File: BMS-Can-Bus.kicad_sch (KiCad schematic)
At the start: 23 parts, among them J1 Conn_01x05, Q3 Q_PMOS_GSD, Q4 Q_PMOS_GSD, Q5 Q_PMOS_GSD, Q6 Q_PMOS_GSD, U1 BQ76952PFB

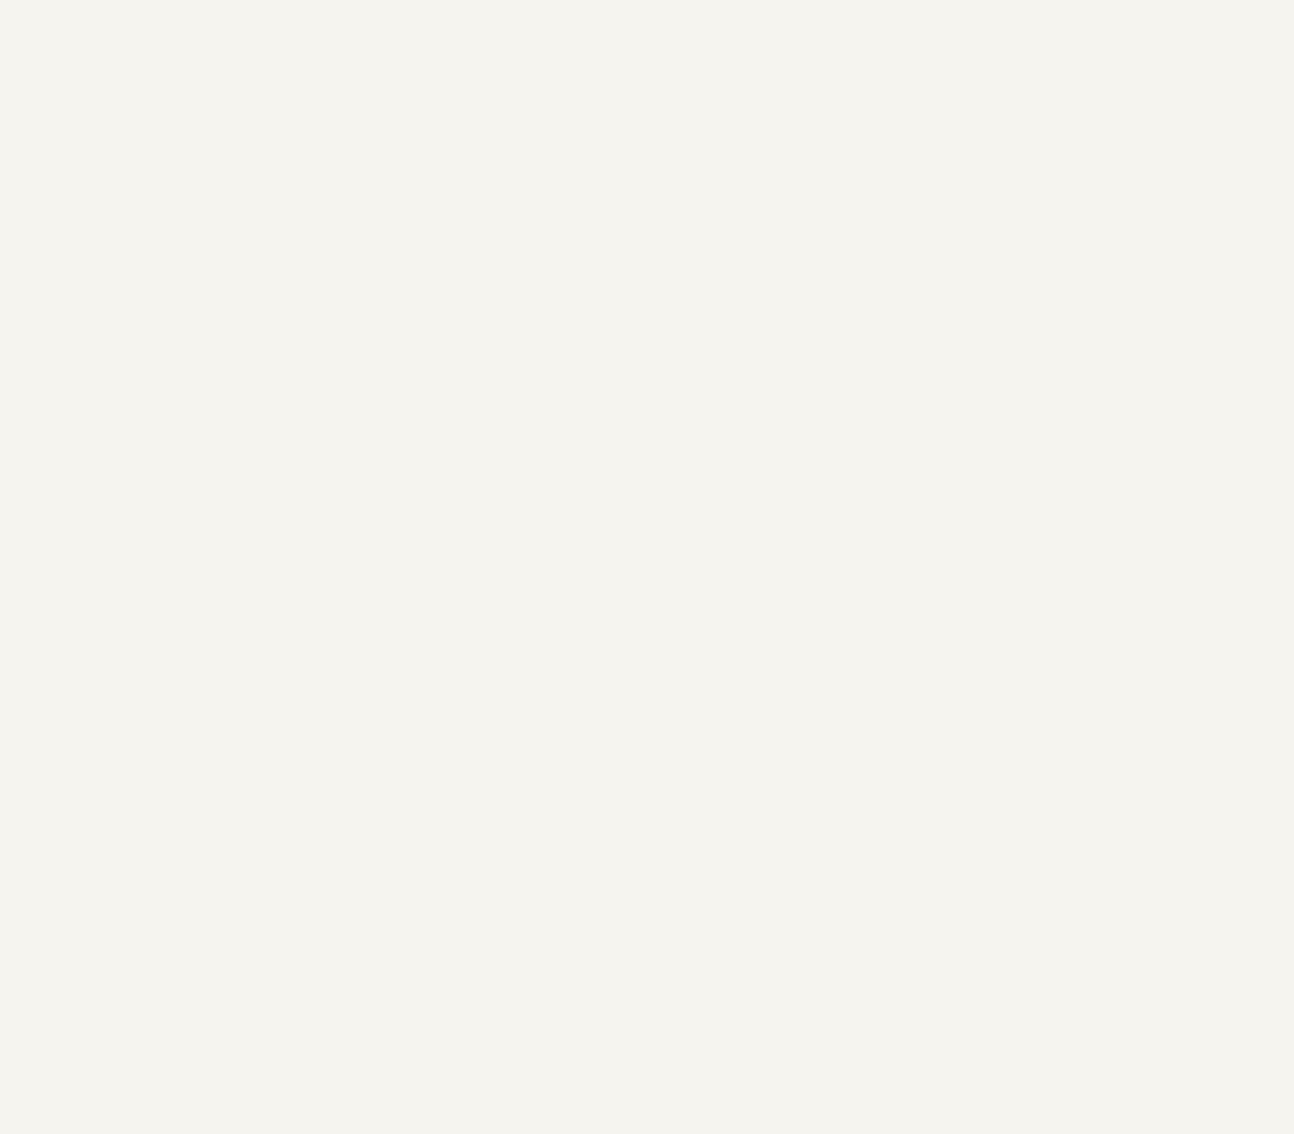
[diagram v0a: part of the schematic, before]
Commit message: Add files via upload
Added STM32 and CAN Bus communication to schematic and PCB.
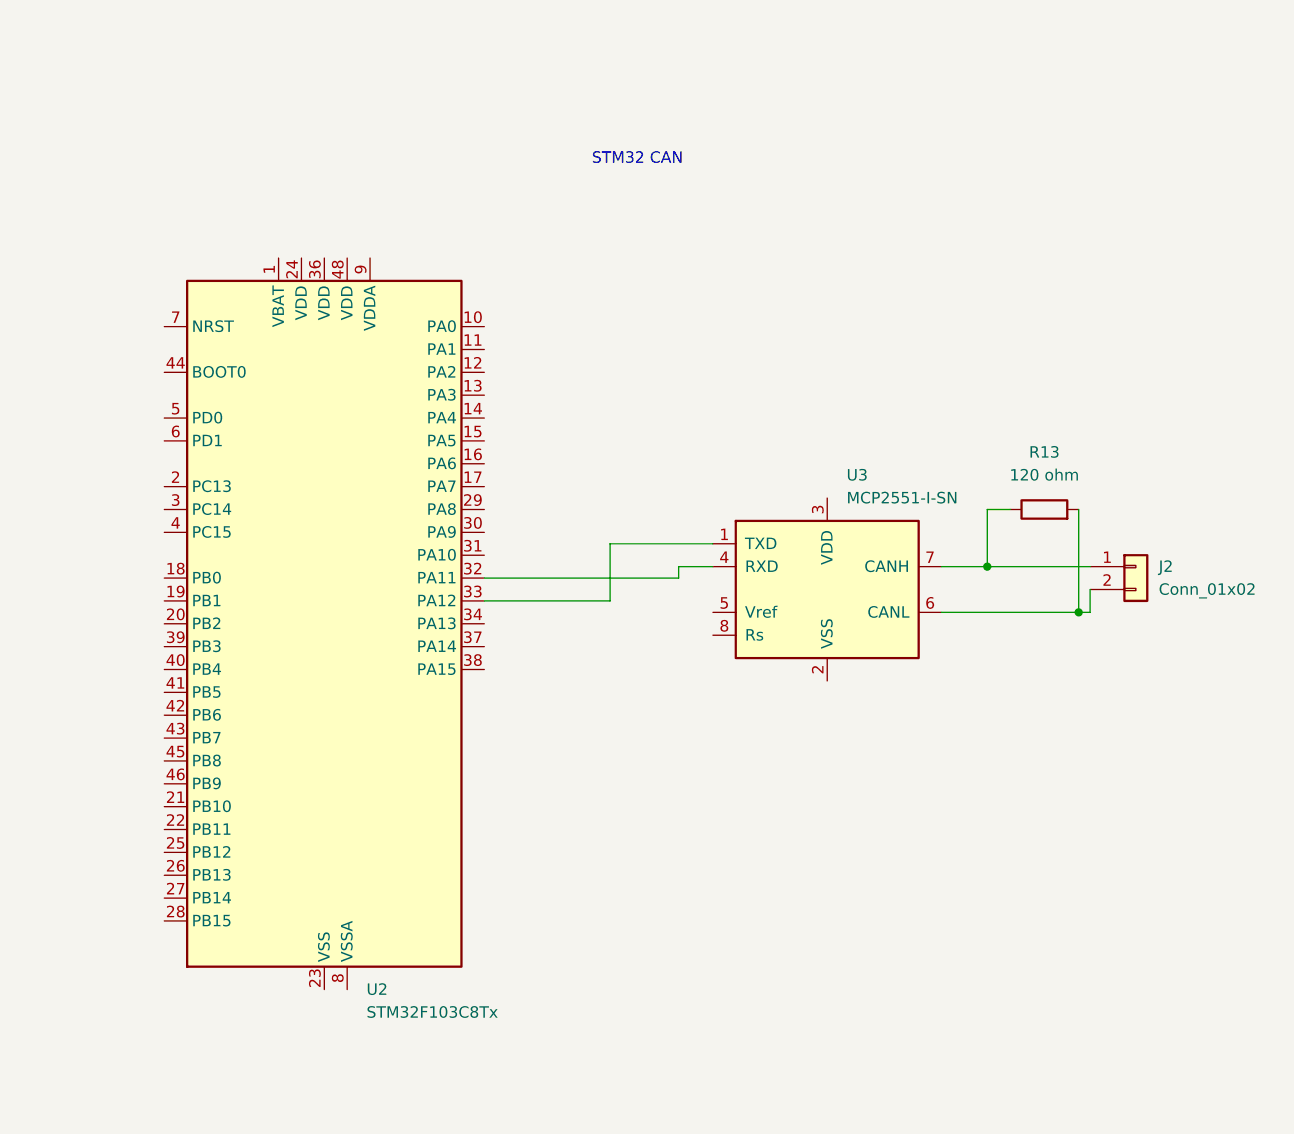
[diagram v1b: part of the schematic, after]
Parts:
- added J2: Conn_01x02, Connector_PinHeader_2.54mm:PinHeader_1x02_P2.54mm_Vertical, symbol Connector_Generic:Conn_01x02
- added R13: 120 ohm, Resistor_SMD:R_0805_2012Metric, symbol Device:R
- added U2: STM32F103C8Tx, Package_QFP:LQFP-48_7x7mm_P0.5mm, symbol MCU_ST_STM32F1:STM32F103C8Tx
- added U3: MCP2551-I-SN, Package_SO:SOIC-8_3.9x4.9mm_P1.27mm, symbol Interface_CAN_LIN:MCP2551-I-SN
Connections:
- new net: U2.33 (PA12), U3.1 (TXD)
- new net: U2.32 (PA11), U3.4 (RXD)
- new net: J2.2 (Pin_2), R13.2, U3.6 (CANL)
- new net: J2.1 (Pin_1), R13.1, U3.7 (CANH)
- new net: U2.23 (VSS), U2.35 (VSS), U2.47 (VSS)
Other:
- note added: "STM32 CAN"

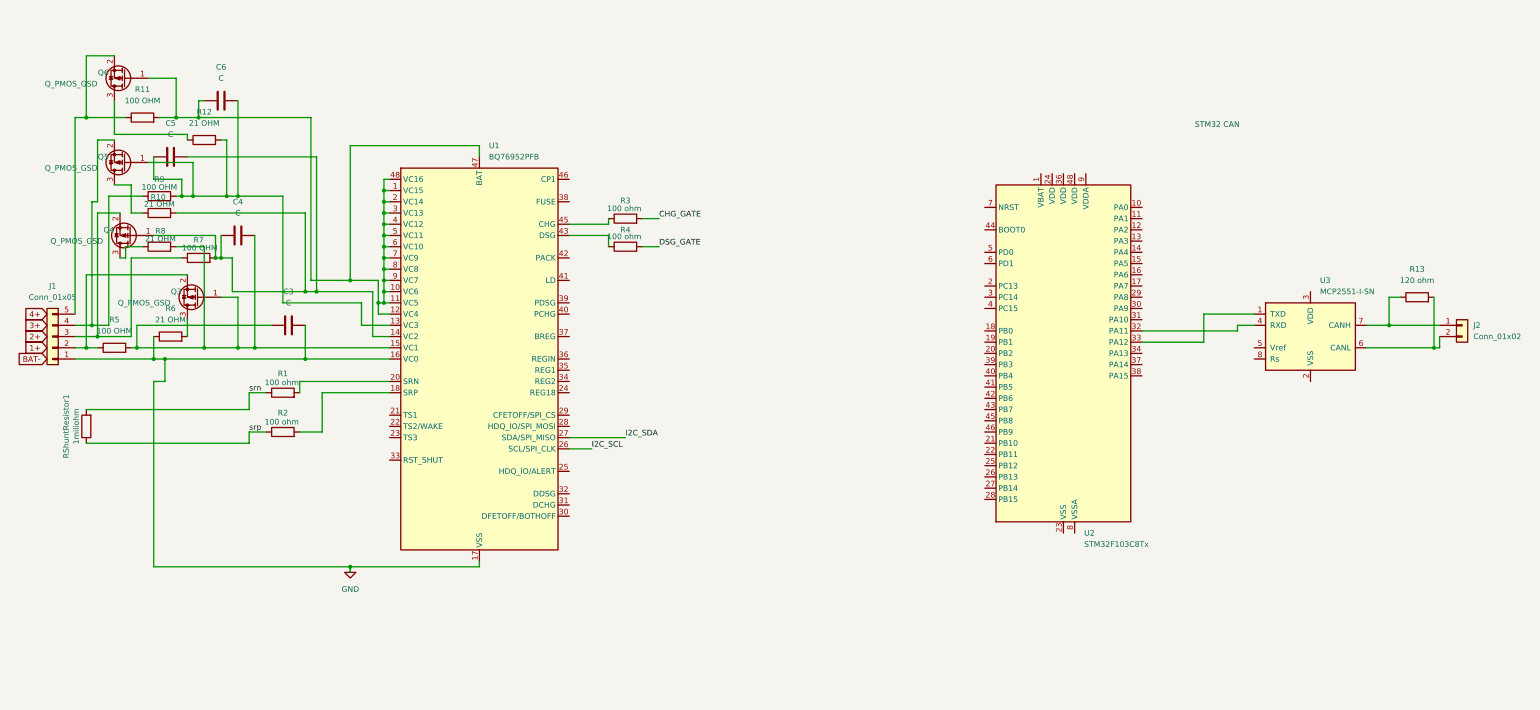
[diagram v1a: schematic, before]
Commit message: Complete STM32 & CAN Bus integration
100A Smart BMS hardware schematics and PCB layout design completed with zero DRC errors.

Key Changes & Technical Implementation:
----------------------------------------
1. STM32F103 Power Supply & Filtering:
   - Tied VBAT, VDD (Pins 24, 36, 48), and VDDA (Pin 9) directly to BQ76952 REG1 (+3V3).
   - Connected VSS (Pin 23) and VSSA (Pin 8) to GND.
   - Added 100nF decoupling capacitors parallel across each VDD-GND pair.

2. HSE Clock, Reset & Boot Configuration:
   - Connected 8MHz external crystal (Y1) across PD0 (Pin 5) and PD1 (Pin 6) with 2x 22pF load capacitors to GND.
   - Configured NRST (Pin 7) with 100nF filter capacitor to GND and 10kΩ pull-up resistor to +3V3.
   - Pulled BOOT0 (Pin 44) to GND via 10kΩ pull-down resistor for internal flash booting.

3. CAN Bus Transceiver Integration (SN65HVD230):
   - Replaced 5V MCP2551 with 3.3V-compatible SN65HVD230 CAN transceiver.
   - Added 100nF decoupling capacitor between VCC (3.3V) and GND.
   - Pulled Rs (Pin 8) to GND via 10kΩ resistor for high-speed operation.
   - Connected TXD/RXD to STM32 PA12/PA11; added 120Ω bus termination resistor across CANH/CANL.

4. Communication & Interrupt Lines:
   - Added 2x 4.7kΩ pull-up resistors (R19, R20) to +3V3 on I2C_SDA (Pin 27) and I2C_SCL (Pin 26).
   - Routed BMS_ALERT interrupt signal (Pin 25) directly to STM32 PA0 (Pin 10).

5. Footprints & PCB Layout (DRC Clean):
   - Assigned TO-220/TO-252 footprints for MOSFETs (Q1, Q2, Q7, Q8), HC-49S for 8MHz crystal, and 2.54mm pin headers for NTCs.
   - Poured continuous GND copper fills on both top (F.Cu) and bottom (B.Cu) layers.
   - Verified Design Rules Check (DRC): 0 Errors, 0 Warnings, 0 Unconnected Items.
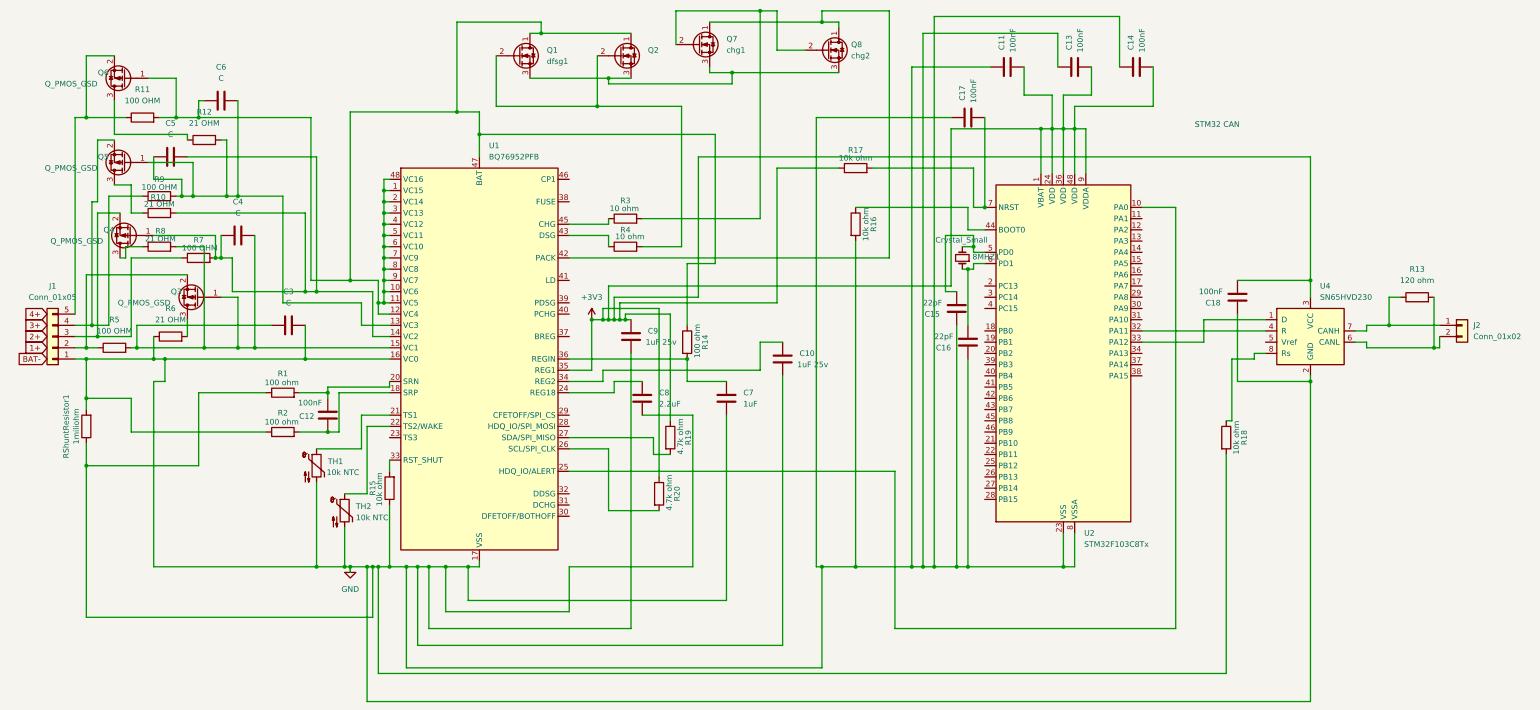
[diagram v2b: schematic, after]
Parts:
- removed U3: MCP2551-I-SN, Package_SO:SOIC-8_3.9x4.9mm_P1.27mm, symbol Interface_CAN_LIN:MCP2551-I-SN
- added 8MHZ1: Crystal_Small, Crystal:Crystal_HC49-4H_Vertical, symbol Device:Crystal_Small
- added C10, C9: 1uF 25v, Capacitor_SMD:C_0603_1608Metric, symbol Device:C
- added C11, C12, C13, C14, C17, C18: 100nF, Capacitor_SMD:C_0603_1608Metric, symbol Device:C
- added C15, C16: 22pF, Capacitor_SMD:C_0603_1608Metric, symbol Device:C
- added C7: 1uF, Capacitor_SMD:C_0603_1608Metric, symbol Device:C
- added C8: 2.2uF, Capacitor_SMD:C_0603_1608Metric, symbol Device:C
- added Q1: dfsg1, Package_TO_SOT_SMD:TO-263-2, symbol Transistor_FET:Q_NMOS_DGS
- added Q2: dsg2, Package_TO_SOT_SMD:TO-263-2, symbol Transistor_FET:Q_NMOS_DGS
- added Q7: chg1, Package_TO_SOT_SMD:TO-263-2, symbol Transistor_FET:Q_NMOS_DGS
- added Q8: chg2, Package_TO_SOT_SMD:TO-263-2, symbol Transistor_FET:Q_NMOS_DGS
- added R14: 100 ohm, Resistor_SMD:R_0805_2012Metric, symbol Device:R
- added R15, R16, R17, R18: 10k ohm, Resistor_SMD:R_0805_2012Metric, symbol Device:R
- added R19, R20: 4.7k ohm, Resistor_SMD:R_0805_2012Metric, symbol Device:R
- added TH1, TH2: 10k NTC, Connector_PinHeader_2.54mm:PinHeader_1x02_P2.54mm_Vertical, symbol Device:Thermistor_NTC
- added U4: SN65HVD230, Package_SO:SOIC-8_3.9x4.9mm_P1.27mm, symbol Interface_CAN_LIN:SN65HVD230
- R3, R4: value 100 ohm -> 10 ohm
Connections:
- net srn is gone; now on net GND: R1.1, RShuntResistor1.2
- net srp is gone; now on net GND: R2.1, RShuntResistor1.1
- net GND: now also U2.23 (VSS), U2.35 (VSS), U2.47 (VSS), U2.8 (VSSA), C10.1, C11.2, C13.2, C14.2, C15.2, C16.2, C17.2, C18.2, C7.1, C8.1, C9.1, R15.1, R16.2, R18.2, TH1.2, TH2.2, U4.2 (GND)
- net at U2.33 (PA12): now also U4.1 (D)
- net at U2.32 (PA11): now also U4.4 (R)
- net at J2.2 (Pin_2), R13.2: now also U4.6 (CANL)
- net at J2.1 (Pin_1), R13.1: now also U4.7 (CANH)
- net at C6.1, Q6.1 (G), R11.2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: now also Q1.1 (D), Q2.1 (D), R14.1
- net at R1.2, U1.20 (SRN): now also C12.1
- net at R2.2, U1.18 (SRP): now also C12.2
- net at U1.21 (TS1): now also TH1.1
- net at U1.22 (TS2/WAKE): now also TH2.1
- net at U1.24 (REG18): now also C8.2
- net at U1.25 (HDQ_IO/ALERT): now also U2.10 (PA0)
- net at U1.33 (RST_SHUT): now also R15.2
- net at U1.34 (REG2): now also C10.2
- net +3V3: now reaches U1.35 (REG1)
- net +3V3: now also U2.1 (VBAT), U2.24 (VDD), U2.36 (VDD), U2.48 (VDD), U2.9 (VDDA), C11.1, C13.1, C14.1, C18.1, C9.2, R17.1, R19.1, R20.1, U4.3 (VCC)
- net at U1.36 (REGIN): now also C7.2, R14.2
- net at U1.42 (PACK): now also Q7.1 (D), Q8.1 (D)
- net at U2.44 (BOOT0): now also R16.1
- net at U2.5 (PD0): now also 8MHZ1.2, C15.1
- net at U2.6 (PD1): now also 8MHZ1.1, C16.1
- net at U2.7 (NRST): now also C17.1, R17.2
- net CHG_GATE: no longer names the net of R3.2
- net CHG_GATE: now also Q7.2 (G), Q8.2 (G)
- net DSG_GATE: no longer names the net of R4.2
- net DSG_GATE: now also Q1.2 (G), Q2.2 (G)
- net I2C_SCL: no longer names the net of U1.26 (SCL/SPI_CLK)
- net I2C_SCL: now also R20.2
- net I2C_SDA: no longer names the net of U1.27 (SDA/SPI_MISO)
- net I2C_SDA: now also R19.2
- new net: Q1.3 (S), Q2.3 (S), Q7.3 (S), Q8.3 (S)
- new net: R18.1, U4.8 (Rs)

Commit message: critical hardware blockers & BQ76952 connections
Applied essential hardware fixes and schematic revisions:

- Linked BQ76952 I2C lines (SDA/SCL) to STM32 (PB6/PB7) with net labels.
- Corrected shunt resistor differential sense connections (SRP/SRN) and added 100nF filter capacitor (C19).
- Added 100nF charge pump capacitor to CP1 pin (Pin 46) for high-side MOSFET driving.
- Added PACK+ connector terminal (J_PACK+1) to the charge/discharge MOSFET output chain.
- Cleaned up CAN transceiver configuration to standard 3.3V SN65HVD230 (U4).
- Prepared high-current power path nodes for 100A polygon fill/copper zones on PCB layout.
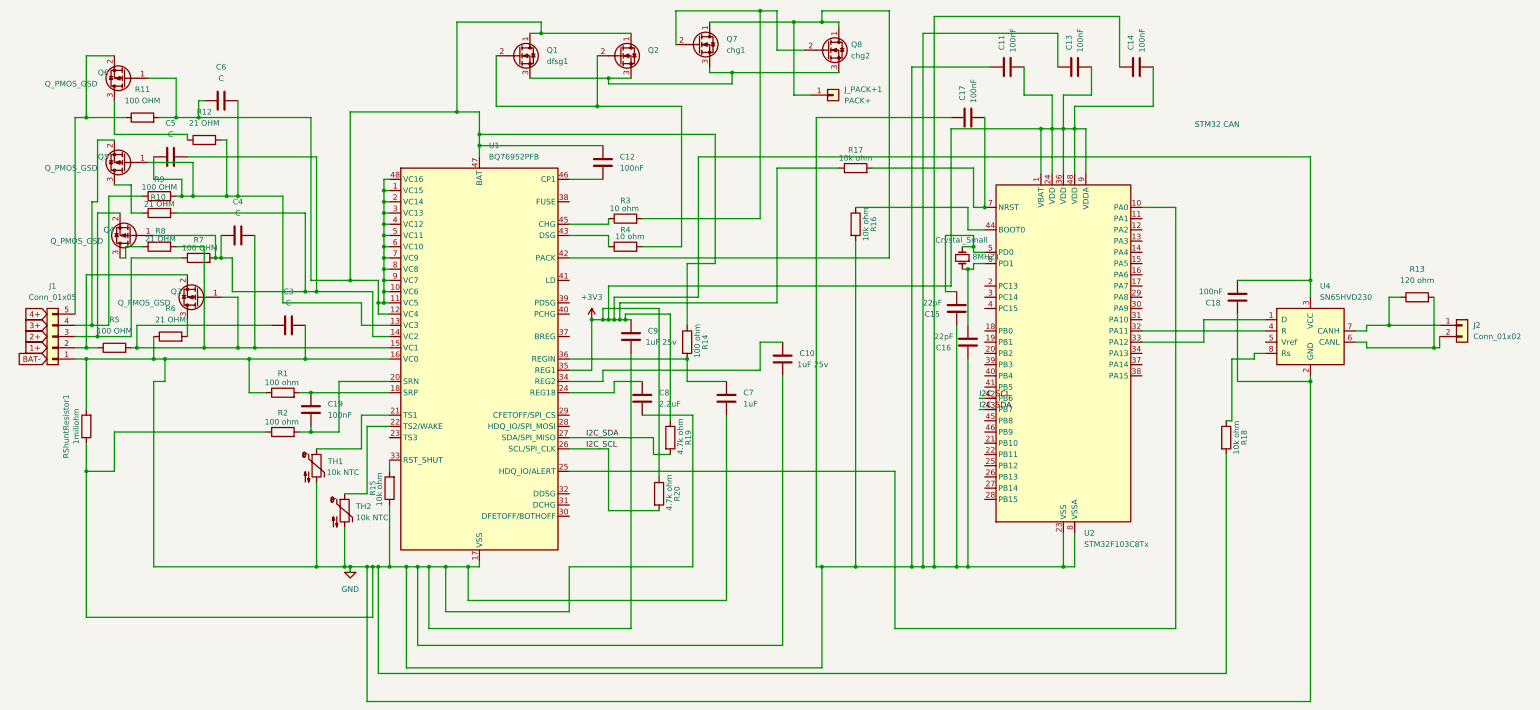
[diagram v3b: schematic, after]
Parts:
- added C19: 100nF, Capacitor_SMD:C_0603_1608Metric, symbol Device:C
- added J_PACK+1: PACK+, MountingHole:MountingHole_5.3mm_M5_Pad, symbol Connector_Generic:Conn_01x01
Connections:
- net at C6.1, Q1.1 (D), Q2.1 (D)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: now also C12.2
- net I2C_SCL: now reaches R20.2, U1.26 (SCL/SPI_CLK)
- net I2C_SCL: now also U2.42 (PB6)
- net at Q7.1 (D), Q8.1 (D), U1.42 (PACK): now also J_PACK+1.1 (Pin_1)
- net I2C_SDA: now reaches R19.2, U1.27 (SDA/SPI_MISO)
- net I2C_SDA: now also U2.43 (PB7)
- net at U1.46 (CP1): now also C12.1
- new net: C19.1, R2.2, U1.20 (SRN)
- new net: C19.2, R1.2, U1.18 (SRP)
